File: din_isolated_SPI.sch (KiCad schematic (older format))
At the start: 19 parts, among them J1 CONN_01X10, U1 SI8661AB-B-IS1, U4 WeMos_mini

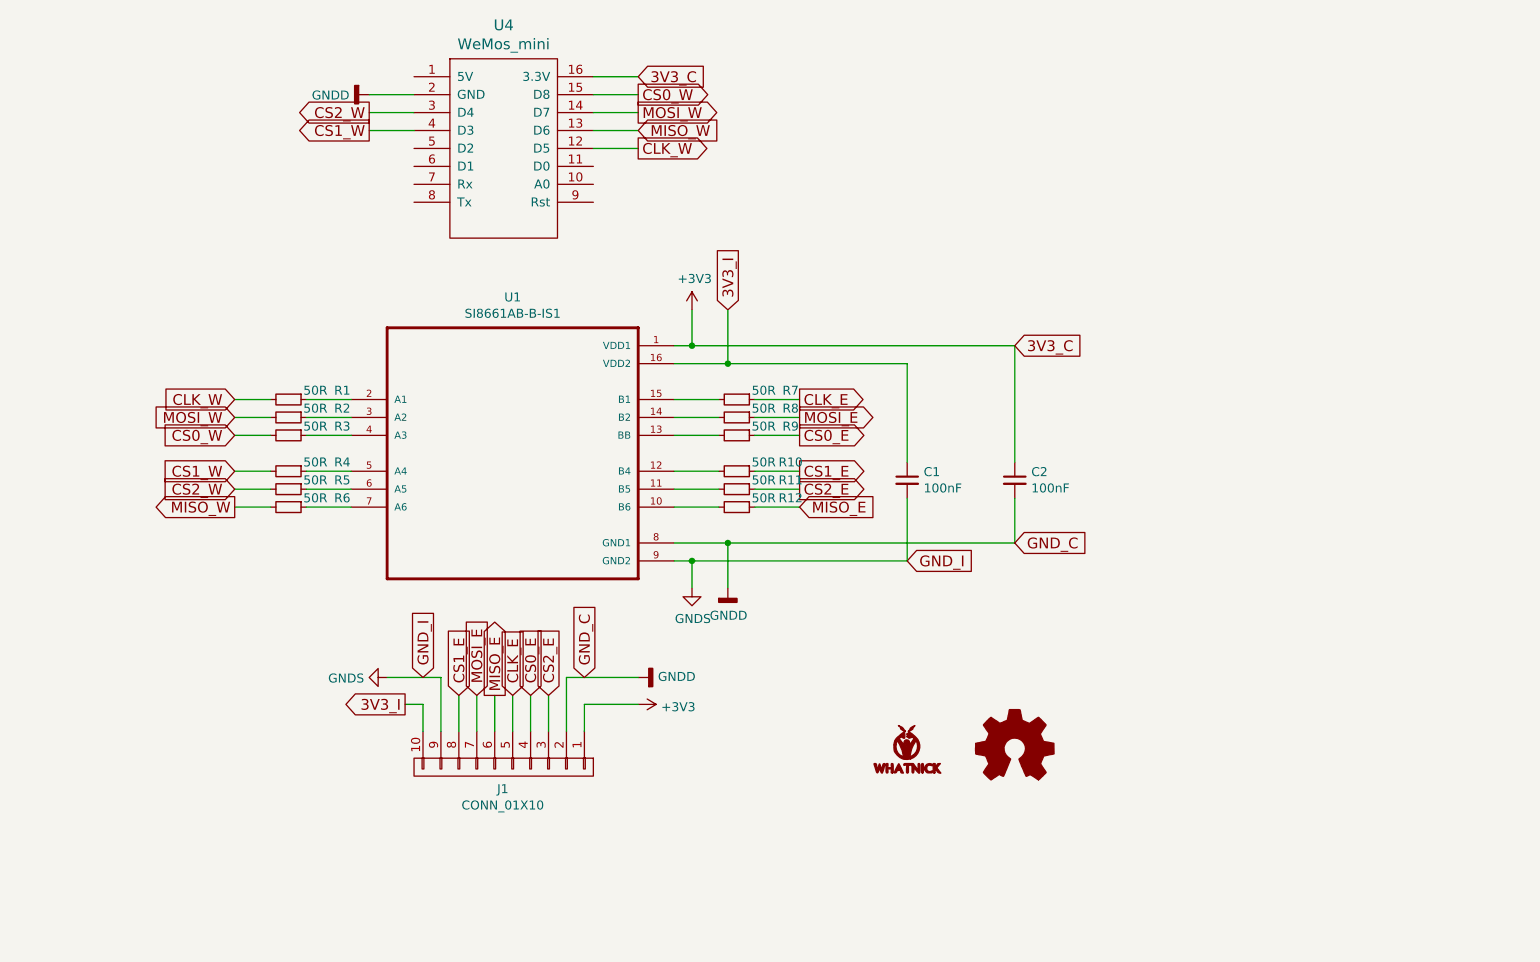
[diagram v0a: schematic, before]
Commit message: updating readme and schematic.
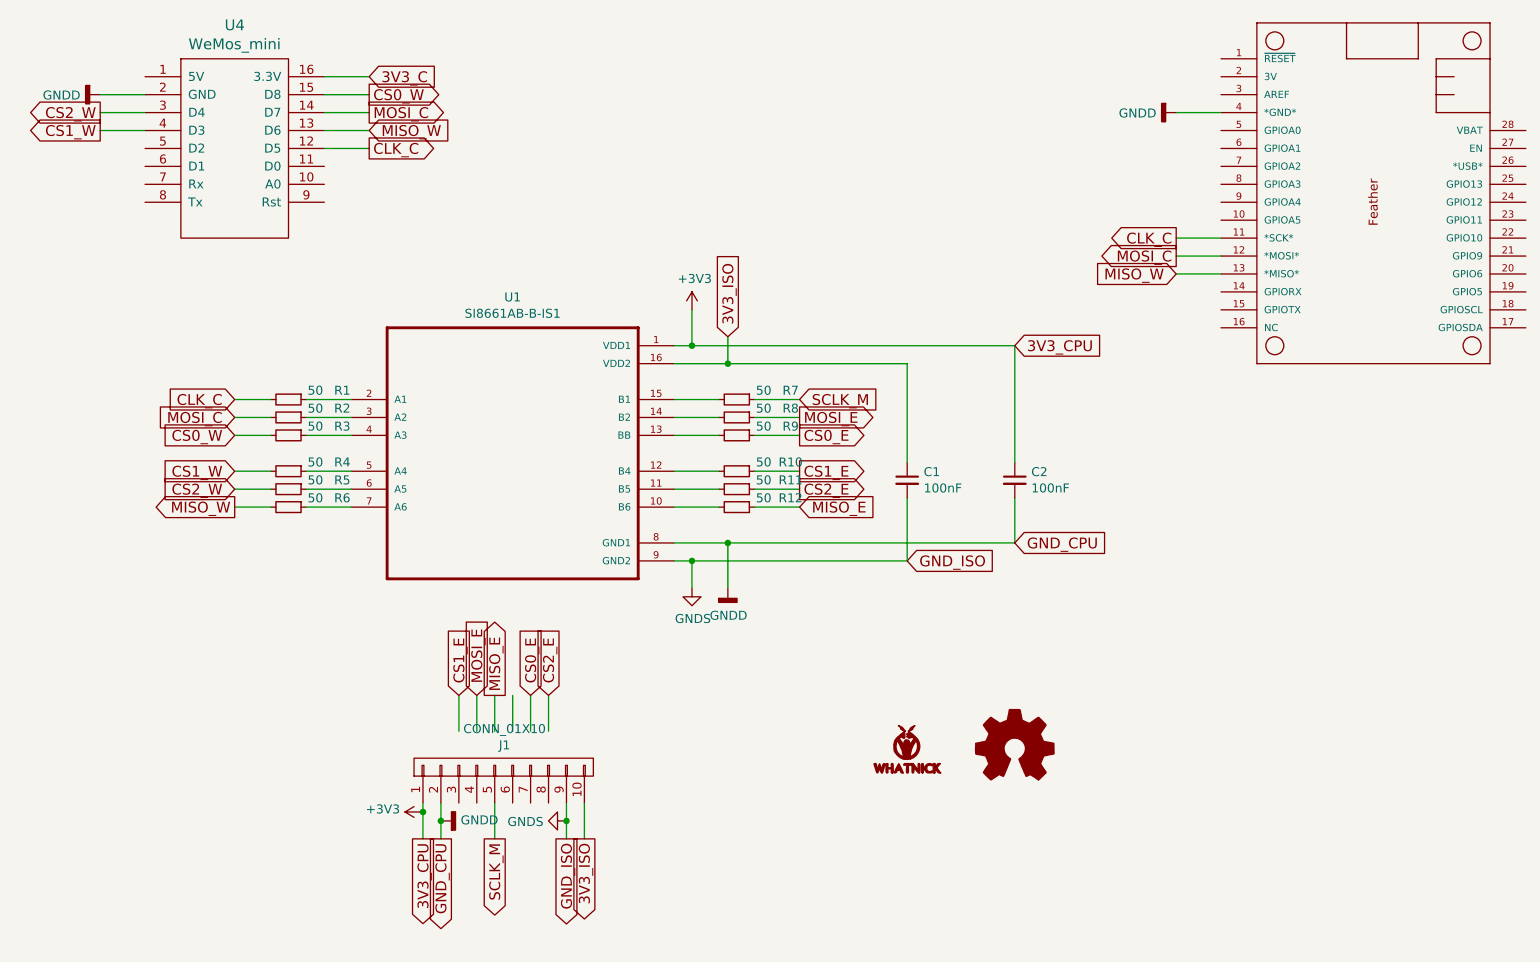
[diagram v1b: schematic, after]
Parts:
- added MS?: ADAFRUIT_FEATHERWING_FitHome, symbol Adafruit_Feather:ADAFRUIT_FEATHERWING_FitHome
- R1, R10, R11, R12, R2, R3, R4, R5, R6, R7, R8, R9: value 50R -> 50
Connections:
- net labels added: 3V3_CPU, 3V3_ISO, CLK_C, GND_CPU, GND_ISO, MOSI_C, SCLK_M
- net labels removed: 3V3_I, CLK_E, CLK_W, GND_C, GND_I, MOSI_W
- wire segments 62 -> 66
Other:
- moved on the sheet: J1, U4
